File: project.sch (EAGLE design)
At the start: 32 parts, among them J2 AUDIO_JACK_3.5MM_KIT, J3 AUDIO_JACK_3.5MM_KIT, J4 AUDIO_JACK_3.5MM_KIT, U1 TL081N, U2 TL081N, X1 736880-49, X2 736880-49

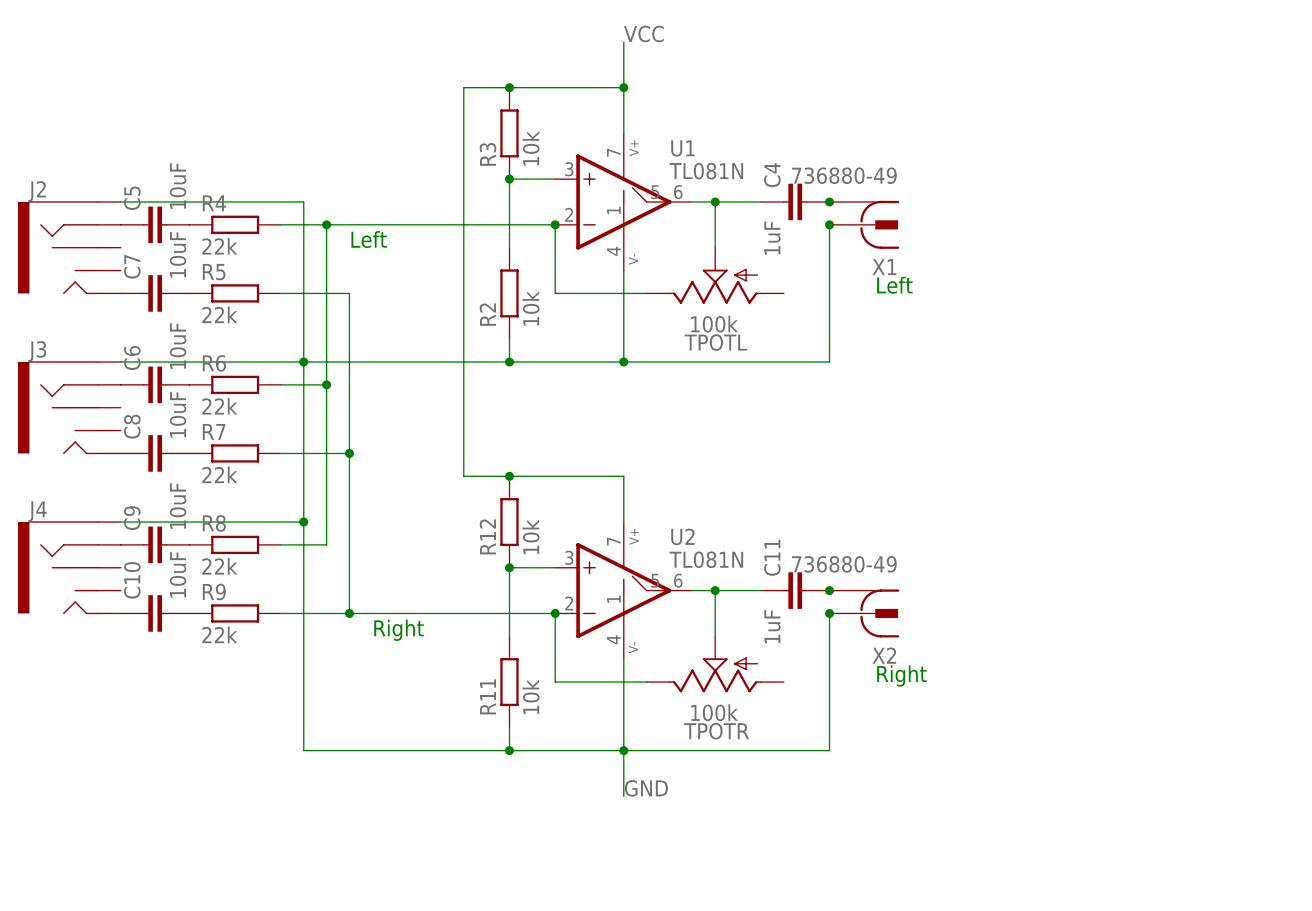
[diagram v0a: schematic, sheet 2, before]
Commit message: Fixing all bugs thus far that were in the schematic. PCB layout now broken!
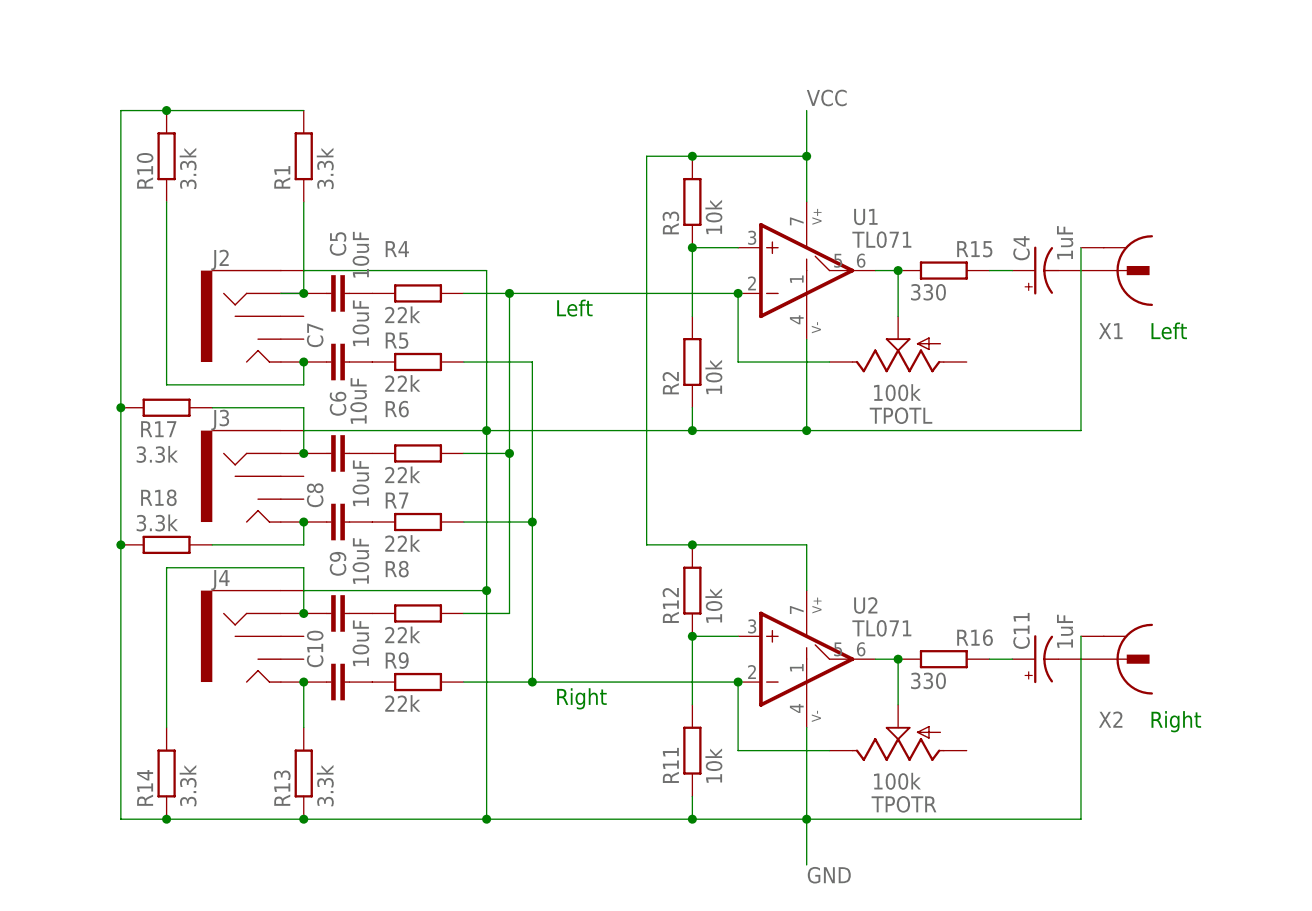
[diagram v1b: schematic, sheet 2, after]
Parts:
- added C12: 10uF, resistor:CPOL-EUCT6032
- added IC1: LM1117LD-3.3, lm1117_11:LM1117LD-3.3
- added R1, R10, R13, R14, R17, R18: 3.3k, resistor:R-EU_0204/5
- added R15, R16: 330, resistor:R-EU_0204/5
- C11, C4: device rcl:C-EU050-024X044 -> SparkFun-Capacitors:10UF-POLAR-RADIAL-2.5MM-25V-20%
- U1, U2: value TL081N -> TL071
- X1, X2: value 736880-49 -> CONRAD_736880-49; device con-conrad:736880-49 -> JRS:CONRAD_736880-49
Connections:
- removed net N$25: C11.2, X2.1
- removed net VBUS: C1.1, J1.VBUS, L1.1
- new net N$1: C4.-, X1.1
- new net N$11: C1.1, C12.+, IC1.IN, J1.VBUS
- new net N$2: C4.+, R15.2
- new net N$3: C11.-, X2.2
- new net N$7: IC1.OUT, L1.1
- net GND: now also C12.-, IC1.GND, R1.2, R10.2, R13.1, R14.1, R17.2, R18.2, X2.1; no longer X2.2
- net N$10: now also R17.1
- net N$12: now also R10.1
- net N$13: now also R18.1
- net N$14: now also R14.2
- net N$15: now also R13.2
- net N$24: now also R16.1; no longer C11.1
- net N$5: now also R15.1; no longer C4.1
- net N$6: now also C11.+, R16.2; no longer C4.2, X1.1
- net N$8: now also R1.1
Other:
- moved on the sheet: C1, C10, C2, C3, C5, C6, C7, C8, C9, J1, J2, J3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

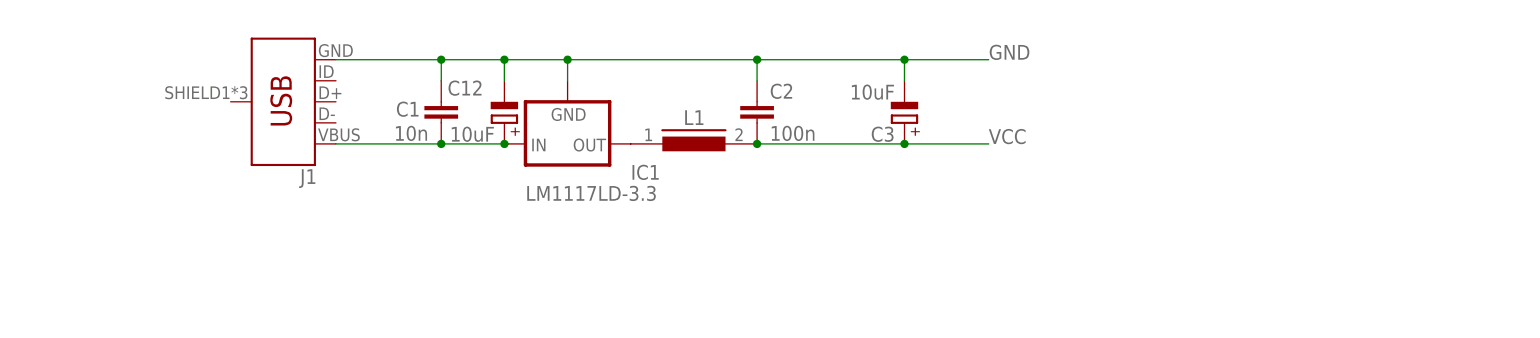
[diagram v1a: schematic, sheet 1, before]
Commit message: Updating with new power supply Rev.
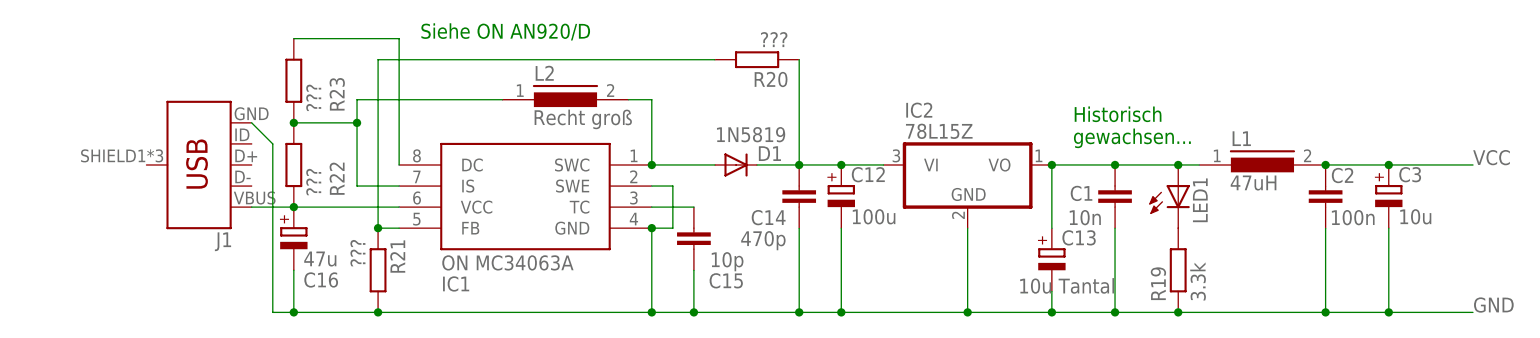
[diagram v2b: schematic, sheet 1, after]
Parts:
- added C13: 10u Tantal, resistor:CPOL-EUE2-4
- added C14: 470p, resistor:C-EU050-024X044
- added C15: 10p, resistor:C-EU050-024X044
- added C16: 47u, resistor:CPOL-EUE2.5-5
- added D1: 1N5819, diode:1N4004
- added IC2: 78L15Z, linear:78L15Z
- added L2: Recht groß, inductors:82114R
- added LED1: (no value), led:LED5MM
- added R19: 3.3k, resistor:R-EU_0207/7
- added R20, R21, R22, R23: ???, resistor:R-EU_0207/7
- C12: value 10uF -> 100u; device resistor:CPOL-EUCT6032 -> resistor:CPOL-EUE2.5-5
- C3: value 10uF -> 10u
- IC1: value LM1117LD-3.3 -> ON MC34063A; device lm1117_11:LM1117LD-3.3 -> mc34063:MC34063AP
- L1: value Ferrite bead -> 47uH; device inductors:MMICC7 -> inductors:MCC10
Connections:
- new net N$22: C1.2, C13.+, IC2.VO, L1.1, LED1.A
- new net N$23: C12.+, C14.2, D1.C, IC2.VI, R20.1
- new net N$25: LED1.C, R19.2
- new net N$26: C15.2, IC1.TC
- new net N$28: IC1.FB, R20.2, R21.1
- new net N$29: C16.+, IC1.VCC, J1.VBUS, R22.1
- new net N$31: IC1.IS, L2.1, R22.2, R23.1
- net GND: now also C1.1, C13.-, C14.1, C15.1, C16.-, IC1.SWE, IC2.GND, R19.1, R21.2; no longer C1.2
- net N$11: now also D1.A, IC1.SWC, L2.2; no longer C1.1, C12.+, IC1.IN, J1.VBUS
- net N$7: now also IC1.DC, R23.2; no longer IC1.OUT, L1.1
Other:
- note added: "Historisch gewachsen..."
- note added: "Siehe ON AN920/D"
- moved on the sheet: C1, C12, C2, C3, J1, L1

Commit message: Updating to latest prototype revision.
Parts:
- removed C15: 10p, resistor:C-EU050-024X044
- removed C16: 47u, resistor:CPOL-EUE2.5-5
- removed R16: 330, resistor:R-EU_0204/5
- removed R17: 3.3k, resistor:R-EU_0204/5
- removed R20, R21, R22, R23: ???, resistor:R-EU_0207/7
- removed TPOTL, TPOTR: 100k, pot:TRIM_US-B25P
- added TRIM_L, TRIM_R: 100k, pot:TRIM_US-B25P
- C1: value 10n -> 47u; device resistor:C-EU050-024X044 -> resistor:CPOL-EUE2.5-5
- C10, C7, C8, C9: value 10uF -> 10u; device rcl:C-EU050-024X044 -> resistor:CPOL-EUE2-4
- C11: value 1uF -> 10u; device SparkFun-Capacitors:10UF-POLAR-RADIAL-2.5MM-25V-20% -> resistor:CPOL-EUE2-4
- C12: value 100u -> 10u; device resistor:CPOL-EUE2.5-5 -> resistor:CPOL-EUE2-4
- C13: value 10u Tantal -> 100u
- C14: value 470p -> 100u; device resistor:C-EU050-024X044 -> resistor:CPOL-EUE2-4
- C2: value 100n -> 10p
- C3: value 10u -> 470p; device resistor:CPOL-EUE2.5-5 -> resistor:C-EU050-024X044
- C4: value 1uF -> 100u; device SparkFun-Capacitors:10UF-POLAR-RADIAL-2.5MM-25V-20% -> resistor:CPOL-EUE2.5-5
- C5: value 10uF -> 10u Tantal; device rcl:C-EU050-024X044 -> resistor:CPOL-EUE2-4
- C6: value 10uF -> 10n; device rcl:C-EU050-024X044 -> resistor:C-EU050-024X044
- L1: value 47uH -> ~20 windings around 4mm ferrite core; device inductors:MCC10 -> inductors:82114R
- L2: value Recht groß -> 47uH; device inductors:82114R -> inductors:MCC10
- R1: value 3.3k -> 180; device resistor:R-EU_0204/5 -> resistor:R-EU_0207/7
- R10: value 3.3k -> 22k
- R11: value 10k -> 22k
- R13, R14: value 3.3k -> 10k
- R15: value 330 -> 10k
- R18: value 3.3k -> 330
- R19: value 3.3k -> 330; device resistor:R-EU_0207/7 -> resistor:R-EU_0204/5
- R2: value 10k -> 1.2; device resistor:R-EU_0204/5 -> resistor:R-EU_0207/7
- R3: value 10k -> 1k; device resistor:R-EU_0204/5 -> resistor:R-EU_0207/7
- R4: value 22k -> 15k; device resistor:R-EU_0204/5 -> resistor:R-EU_0207/7
- R5: value 22k -> 3.3k; device resistor:R-EU_0204/5 -> resistor:R-EU_0207/7
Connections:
- new net N$33: R11.2, R7.2, R9.2, TRIM_R.E, U2A.-IN
- net GND: now also C1.-, C3.1, C4.-, C5.-, C6.1, R15.1, R3.2, R5.1, X2.2; no longer C1.1, C12.-, C13.-, C14.1, C15.1, C16.-, C3.-, J1.GND, R1.2, R10.2, R11.1, R14.1, R17.2, R18.2, R19.1, R2.1, R21.2, X2.1
- net N$1: now also C13.-; no longer C4.-
- net N$10: now also C8.+, J2.TIP; no longer C6.1, J3.RING, R17.1
- net N$11: now also L1.2; no longer L2.2
- net N$12: now also R10.2, R6.2, R8.2, TRIM_L.E, U1A.-IN; no longer C7.1, J2.TIP, R10.1
- net N$13: now also C8.-, R7.1; no longer C8.1, J3.TIP, R18.1
- net N$14: now also C9.+, J3.RING; no longer C9.1, J4.RING, R14.2
- net N$15: now also C9.-, R8.1; no longer C10.1, J4.TIP, R13.2
- net N$16: now also C10.+, J3.TIP; no longer C5.2, R4.1
- net N$17: now also C10.-, R9.1; no longer C7.2, R5.1
- net N$18: now also C11.+, J4.RING; no longer C6.2, R6.1
- net N$19: now also C11.-, R10.1; no longer C8.2, R7.1
- net N$2: now also C13.+, R18.2; no longer C4.+, R15.2
- net N$20: now also C12.+, J4.TIP; no longer C9.2, R8.1
- net N$21: now also C12.-, R11.1; no longer C10.2, R9.1
- net N$22: now also C5.+, C6.2, L2.1; no longer C1.2, C13.+, L1.1
- net N$23: now also C3.2, C4.+, R4.1; no longer C12.+, C14.2, R20.1
- net N$24: now also R19.1, TRIM_R.S; no longer R16.1, TPOTR.S
- net N$25: now also R5.2; no longer R19.2
- net N$26: now also C2.2; no longer C15.2
- net N$27: now also R14.1, R15.2; no longer R11.2, R12.1
- net N$28: now also R3.1, R4.2; no longer R20.2, R21.1
- net N$29: now also C1.+, R2.1; no longer C16.+, R22.1
- net N$3: now also C14.-, X2.1; no longer C11.-, X2.2
- net N$30: now also J1.GND; no longer R5.2, R7.2, R9.2, TPOTR.E, U2A.-IN
- net N$31: now also L1.1, R1.1, R2.2; no longer L2.1, R22.2, R23.1
- net N$4: now also C7.-, R6.1; no longer R4.2, R6.2, R8.2, TPOTL.E, U1A.-IN
- net N$5: now also R18.1, TRIM_L.S; no longer R15.1, TPOTL.S
- net N$6: now also C14.+, R19.2; no longer C11.+, R16.2
- net N$7: now also R1.2; no longer R23.2
- net N$8: now also C7.+; no longer C5.1, R1.1
- net N$9: now also R12.1, R13.2; no longer R2.2, R3.1
- net VCC: now also L2.2, R14.2; no longer C2.2, C3.+, L1.2, R3.2
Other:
- note added: "See ON Application Note "AN920/D""
- note added: "While circuit is unpowered, just acts like a resistor."
- note removed: "Historisch gewachsen..."
- note removed: "Siehe ON AN920/D"
- moved on the sheet: C11, C2, J1, J2, J3, J4, L1, L2, R10, R11, R12, R13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
